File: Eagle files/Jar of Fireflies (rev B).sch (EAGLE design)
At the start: 18 parts, among them IC1 ATTINY85, J1 POWER_JACKPTH, J3 M02PTH, J4 M02PTH

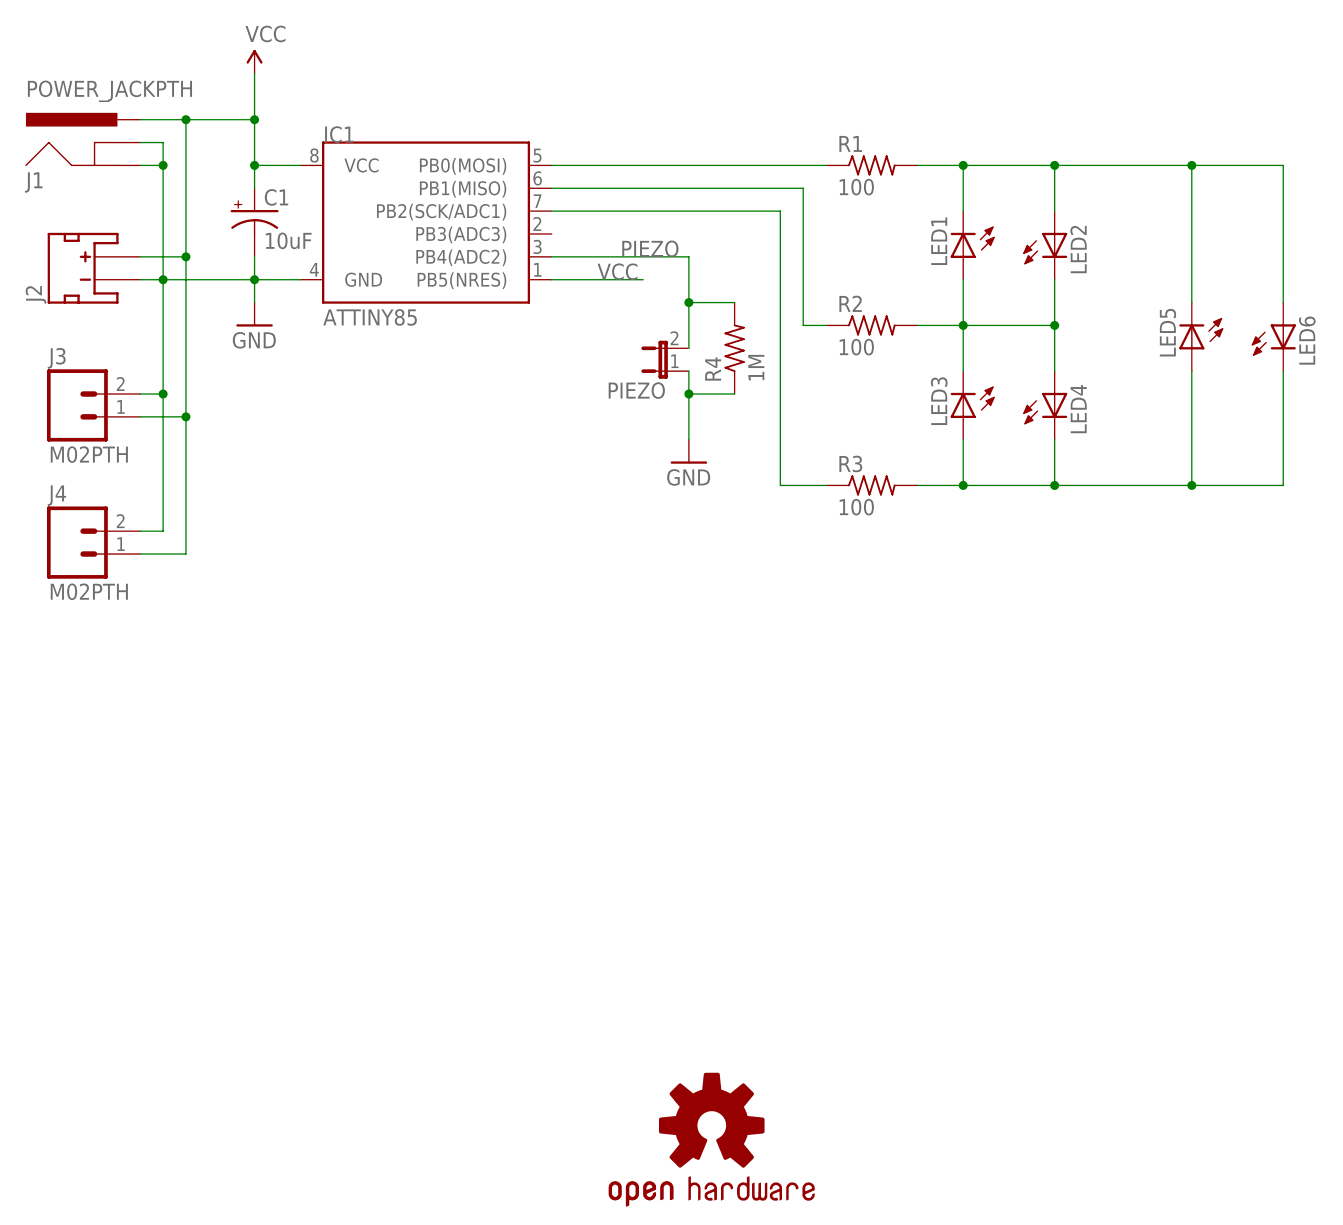
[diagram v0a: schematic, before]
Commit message: Updated Eagle files
Better silkscreen, more power options.
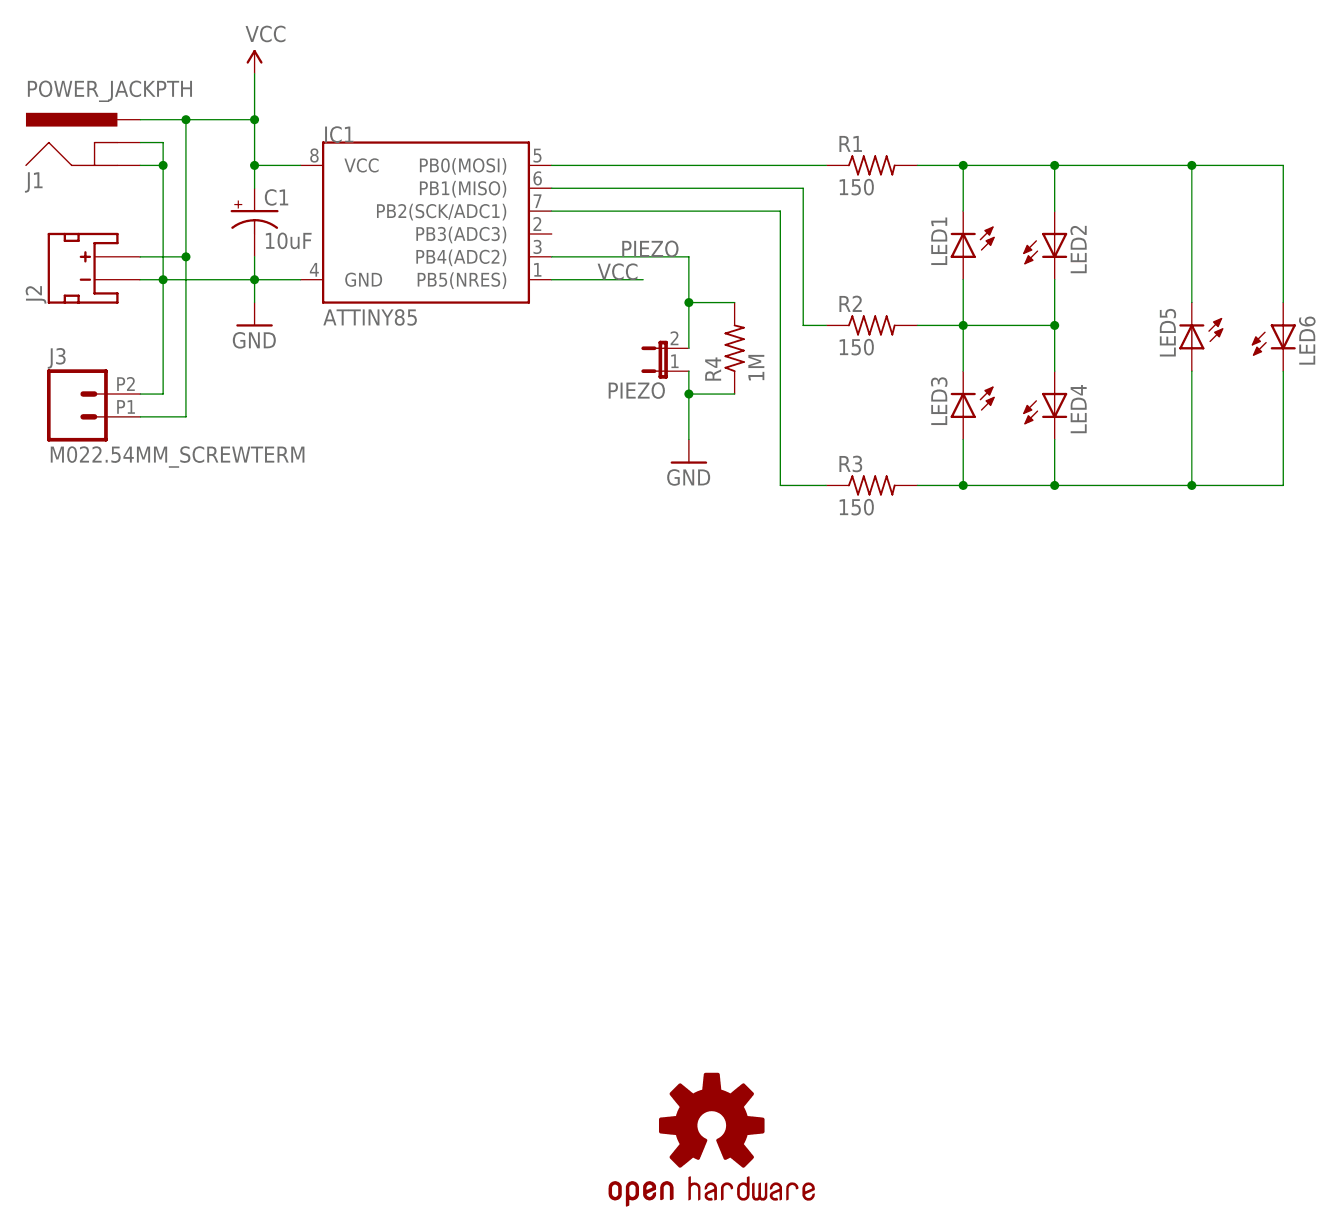
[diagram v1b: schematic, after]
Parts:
- removed J4: M02PTH, SparkFun-Connectors:M02PTH
- J3: value M02PTH -> M022.54MM_SCREWTERM; device SparkFun-Connectors:M02PTH -> SparkFun-Connectors:M022.54MM_SCREWTERM
- R1, R2, R3: value 100 -> 150
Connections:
- net GND: no longer J4.2
- net VCC: no longer J4.1
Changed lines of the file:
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@@
 <?xml version="1.0" encoding="utf-8"?>
 <!DOCTYPE eagle SYSTEM "eagle.dtd">
-<eagle version="6.5.0">
+<eagle version="7.1.0">
 <drawing>
 <settings>
@@
 <part name="LED5" library="SparkFun" deviceset="LED" device="5MM"/>
 <part name="LED6" library="SparkFun" deviceset="LED" device="5MM"/>
-<part name="R1" library="resistor" deviceset="R-US_" device="0207/2V" value="100"/>
-<part name="R2" library="resistor" deviceset="R-US_" device="0204/7" value="100"/>
-<part name="R3" library="resistor" deviceset="R-US_" device="0207/2V" value="100"/>
+<part name="R1" library="resistor" deviceset="R-US_" device="0207/2V" value="150"/>
+<part name="R2" library="resistor" deviceset="R-US_" device="0204/7" value="150"/>
+<part name="R3" library="resistor" deviceset="R-US_" device="0207/2V" value="150"/>
 <part name="GND2" library="supply1" deviceset="GND" device=""/>
 <part name="J1" library="SparkFun-Connectors" deviceset="POWER_JACK" device="PTH"/>
 <part name="J2" library="SparkFun-Connectors" deviceset="JST_2MM_MALE" device=""/>
 <part name="C1" library="SparkFun-Capacitors" deviceset="CAP_POL" device="PTH2" value="10uF"/>
-<part name="J3" library="SparkFun-Connectors" deviceset="M02" device="PTH"/>
-<part name="LOGO1" library="SparkFun-Aesthetics" deviceset="OSHW-LOGO" device="L" value="OSHW-LOGOL"/>
-<part name="J4" library="SparkFun-Connectors" deviceset="M02" device="PTH"/>
+<part name="J3" library="SparkFun-Connectors" deviceset="M02" device="2.54MM_SCREWTERM"/>
+<part name="LOGO1" library="SparkFun-Aesthetics" deviceset="OSHW-LOGO" device="L"/>
 </parts>
 <sheets>
@@
 <instance part="J3" gate="G$1" x="60.96" y="91.44"/>
 <instance part="LOGO1" gate="G$1" x="132.08" y="12.7"/>
-<instance part="J4" gate="G$1" x="60.96" y="76.2"/>
 </instances>
 <busses>
@@
 <pinref part="C1" gate="G$1" pin="-"/>
 <wire x1="81.28" y1="106.68" x2="81.28" y2="109.22" width="0.1524" layer="91"/>
-<pinref part="J3" gate="G$1" pin="2"/>
 <wire x1="68.58" y1="93.98" x2="71.12" y2="93.98" width="0.1524" layer="91"/>
 <wire x1="71.12" y1="93.98" x2="71.12" y2="106.68" width="0.1524" layer="91"/>
-<wire x1="71.12" y1="93.98" x2="71.12" y2="78.74" width="0.1524" layer="91"/>
-<junction x="71.12" y="93.98"/>
-<pinref part="J4" gate="G$1" pin="2"/>
-<wire x1="71.12" y1="78.74" x2="68.58" y2="78.74" width="0.1524" layer="91"/>
+<pinref part="J3" gate="G$1" pin="2"/>
 </segment>
 <segment>
@@
 <wire x1="81.28" y1="116.84" x2="81.28" y2="119.38" width="0.1524" layer="91"/>
 <junction x="81.28" y="119.38"/>
-<pinref part="J3" gate="G$1" pin="1"/>
 <wire x1="68.58" y1="91.44" x2="73.66" y2="91.44" width="0.1524" layer="91"/>
 <wire x1="73.66" y1="91.44" x2="73.66" y2="109.22" width="0.1524" layer="91"/>
-<pinref part="J4" gate="G$1" pin="1"/>
-<wire x1="68.58" y1="76.2" x2="73.66" y2="76.2" width="0.1524" layer="91"/>
-<wire x1="73.66" y1="76.2" x2="73.66" y2="91.44" width="0.1524" layer="91"/>
-<junction x="73.66" y="91.44"/>
-</segment>
-<segment>
+<pinref part="J3" gate="G$1" pin="1"/>
+</segment>
+<segment>
